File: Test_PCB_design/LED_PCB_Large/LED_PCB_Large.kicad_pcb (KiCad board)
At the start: 2 copper layers, 24 x 24 mm, 113 parts, among them J1 AS150UPB 2+4, Q1 BUK9Y107-80EX, Q10 BUK9Y107-80EX, Q11 BUK9Y107-80EX, Q12 BUK9Y107-80EX, Q2 BUK9Y107-80EX, Q3 BUK9Y107-80EX, Q4 BUK9Y107-80EX, Q5 BUK9Y107-80EX, Q6 BUK9Y107-80EX, Q7 BUK9Y107-80EX, Q8 BUK9Y107-80EX, Q9 BUK9Y107-80EX, U1 MAX20078ATE_V_T, U2 MAX20078ATE_V_T, U3 MAX20078ATE_V_T, U4 MAX20078ATE_V_T, U5 MAX20078ATE_V_T, U6 MAX20078ATE_V_T

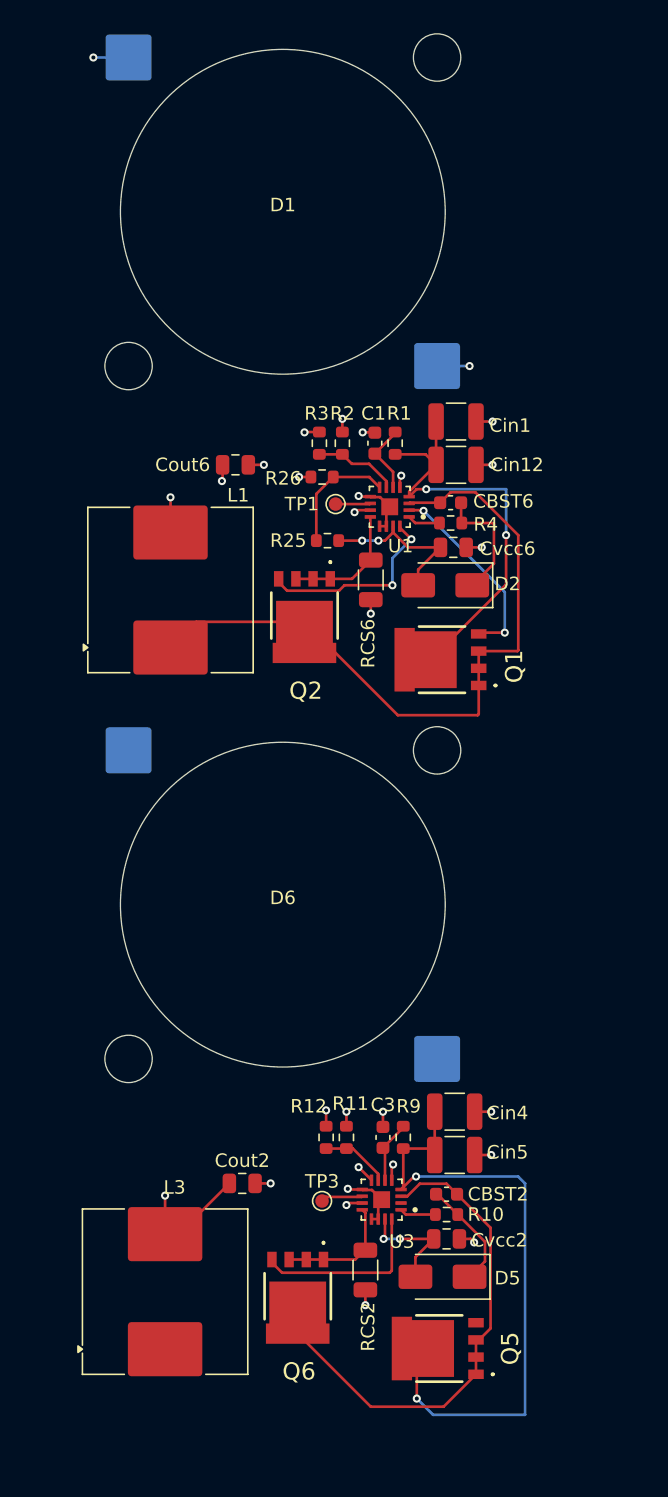
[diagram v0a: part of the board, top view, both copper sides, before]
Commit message: updated LED1 with traces
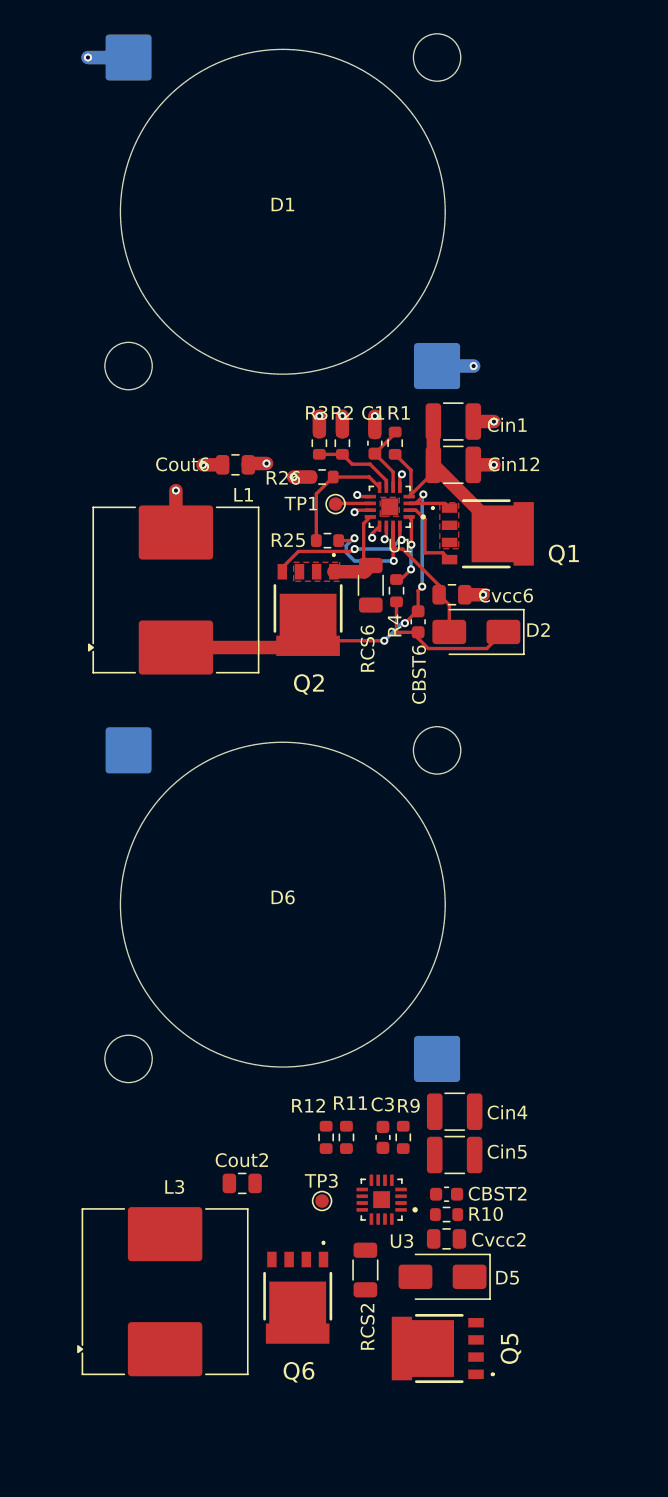
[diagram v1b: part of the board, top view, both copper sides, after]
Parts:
- moved Q1 9.86 mm to (114.5, 54.8), turned to -90 degrees
- moved CBST6 9.12 mm to (109.5, 61.3), turned to 90 degrees
- moved R4 6.40 mm to (107.9, 59.0), turned to -90 degrees
- moved D2 4.15 mm to (113.8, 62.0)
- moved Cvcc6 3.50 mm to (112.0, 59.3)
- moved Q2 0.59 mm to (101.4, 60.3)
- moved RCS6 0.40 mm to (106.0, 58.6)
- moved L1 0.40 mm to (91.6, 59.0)
- moved Cin1 0.20 mm to (112.1, 46.5)
- moved Cin12 0.20 mm to (112.1, 49.7)
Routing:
- net +48V_FUSED: track 80.2 -> 16.9 mm, vias 4 -> 0
- net Net-(Q5-S_1): track 36.2 -> 0.00 mm
- net Net-(Q1-S_1): track 52.3 -> 33.5 mm, vias 0 -> 4
- net GND: track 28.9 -> 14.9 mm, vias 18 -> 11
- net Net-(Q6-G): track 13.3 -> 0.00 mm
- net Net-(Q6-S_1): track 9.00 -> 0.00 mm
- net /LED+: track 17.6 -> 8.73 mm, vias 6 -> 4
- net Net-(Q1-G): track 14.5 -> 5.96 mm, vias 2 -> 0
- net Net-(D5-A): track 8.57 -> 0.00 mm, vias 2 -> 0
- net Net-(D5-K): track 8.28 -> 0.00 mm
- net Net-(D2-A): track 12.2 -> 18.8 mm
- net Net-(U3-OUT): track 5.09 -> 0.00 mm
- net Net-(U3-TON): track 4.67 -> 0.00 mm
- net Net-(Q2-G): track 14.5 -> 11.1 mm
- net /IOUTV3: track 3.11 -> 0.00 mm
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- added copper zone on F.Cu, net GND
- added copper zone on F.Cu, net Net-(Q1-S_1)
- added copper zone on F.Cu, net Net-(Q2-S_1)

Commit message: updated with all LED traces
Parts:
- moved L2 285.3 mm to (155.2, 58.6), turned to 90 degrees
- moved Q4 284.3 mm to (145.5, 60.4), turned to 180 degrees
- moved L4 280.5 mm to (155.2, 105.9), turned to 90 degrees
- moved L6 276.2 mm to (154.2, 153.0), turned to 90 degrees
- moved J1 274.6 mm to (123.9, 6.70), turned to 180 degrees
- moved Q8 262.0 mm to (145.5, 107.6), turned to 180 degrees
- moved U2 261.8 mm to (142.8, 52.8), turned to 180 degrees
- moved Q7 258.9 mm to (132.4, 102.9), turned to 90 degrees
- moved Q3 256.5 mm to (132.4, 55.0), turned to 90 degrees
- moved R8 249.8 mm to (146.3, 48.3), turned to 90 degrees
- moved C2 249.0 mm to (140.5, 48.3), turned to -90 degrees
- moved Cout1 248.5 mm to (151.8, 48.4), turned to 180 degrees
- moved R7 246.6 mm to (144.2, 48.3), turned to -90 degrees
- moved CBST1 246.2 mm to (137.5, 61.2), turned to 90 degrees
- moved U4 245.5 mm to (142.6, 100.2), turned to 180 degrees
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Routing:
- net +48V_FUSED: track 16.9 -> 101.8 mm, vias 0 -> 6
- net GND: track 14.9 -> 97.5 mm, vias 11 -> 66
- net /LED+: track 8.73 -> 50.6 mm, vias 4 -> 24
- net Net-(Q11-S_1): track 0.00 -> 39.9 mm
- net Net-(Q3-S_1): track 0.00 -> 39.9 mm, vias 0 -> 2
- net Net-(Q7-S_1): track 0.00 -> 39.2 mm, vias 0 -> 2
- net Net-(Q10-D_1): track 0.00 -> 33.4 mm, vias 0 -> 4
- net Net-(Q5-S_1): track 0.00 -> 33.0 mm, vias 0 -> 4
- net Net-(D7-A): track 0.00 -> 17.2 mm, vias 0 -> 4
- net Net-(D11-A): track 0.00 -> 15.3 mm, vias 0 -> 2
- net Net-(D3-A): track 0.00 -> 15.2 mm, vias 0 -> 2
- net Net-(D11-K): track 0.00 -> 13.2 mm, vias 0 -> 2
- net Net-(Q7-G): track 0.00 -> 12.3 mm, vias 0 -> 2
- net Net-(Q3-G): track 0.00 -> 12.3 mm, vias 0 -> 2
- net Net-(D3-K): track 0.00 -> 12.3 mm
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- added copper zone on F.Cu, net +48V_FUSED
- added copper zone on B.Cu, net GND
- added copper zone on F.Cu, net Net-(Q10-D_1)
- added copper zone on F.Cu, net Net-(Q10-S_1)
- added copper zone on F.Cu, net Net-(Q11-S_1)
- added copper zone on F.Cu, net Net-(Q12-S_1)
- added copper zone on F.Cu, net Net-(Q3-S_1)
- added copper zone on F.Cu, net Net-(Q4-S_1)
- added copper zone on F.Cu, net Net-(Q5-S_1)
- added copper zone on F.Cu, net Net-(Q6-S_1)
- added copper zone on F.Cu, net Net-(Q7-S_1)
- added copper zone on F.Cu, net Net-(Q8-S_1)
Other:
- board size 24 x 24 mm -> 88.7 x 182.4 mm

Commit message: updated everything just need to check electrical traces to make sure they work.
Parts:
- moved R2 8.28 mm to (96.0, 46.4), turned to 0 degrees
- moved R7 8.13 mm to (151.7, 45.1), turned to 180 degrees
- moved R11 7.83 mm to (97.9, 92.7), turned to 0 degrees
- moved F1 6.87 mm to (118.0, 20.3), turned to 90 degrees
- moved R23 6.56 mm to (151.5, 139.7), turned to 180 degrees
- moved R19 6.27 mm to (95.6, 139.5), turned to 0 degrees
- moved R15 5.70 mm to (150.4, 93.3), turned to 180 degrees
- moved C7 4.30 mm to (121.2, 27.9), turned to -90 degrees
- moved R3 1.70 mm to (104.1, 48.1)
- moved R8 1.23 mm to (145.2, 47.8)
- moved J1 0.40 mm to (123.5, 6.70)
- turned Cout5 to 180 degrees
- turned D1 to 90 degrees
- turned D10 to 90 degrees
- turned D12 to 180 degrees
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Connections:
- Cout1 pad 1: /LED+ -> /LED2+
- Cout2 pad 1: /LED+ -> /LED3+
- Cout3 pad 1: /LED+ -> /LED4+
- Cout4 pad 1: /LED+ -> /LED5+
- Cout5 pad 1: /LED+ -> /LED6+
- Cout6 pad 1: /LED+ -> /LED1+
- D1 pad 2: /LED+ -> /LED1+
- D10 pad 2: /LED+ -> /LED5+
- D12 pad 2: /LED+ -> /LED6+
- D4 pad 2: /LED+ -> /LED2+
- D6 pad 2: /LED+ -> /LED3+
- D8 pad 2: /LED+ -> /LED4+
- L1 pad 2: /LED+ -> /LED1+
- L2 pad 2: /LED+ -> /LED2+
- L3 pad 2: /LED+ -> /LED3+
- L4 pad 2: /LED+ -> /LED4+
- L5 pad 2: /LED+ -> /LED5+
- L6 pad 2: /LED+ -> /LED6+
- R11 pad 1: /LED+ -> /LED3+
- R15 pad 1: /LED+ -> /LED4+
- R19 pad 1: /LED+ -> /LED5+
- R2 pad 1: /LED+ -> /LED1+
- R23 pad 1: /LED+ -> /LED6+
- R7 pad 1: /LED+ -> /LED2+
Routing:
- net /FAULT: track 8.25 -> 386.0 mm, vias 6 -> 9
- net /PWM: track 9.17 -> 359.0 mm, vias 6 -> 7
- net /REF_1V2: track 21.1 -> 317.1 mm, vias 5 -> 13
- net /LED+: track 50.6 -> 0.00 mm, vias 24 -> 0
- net +48V_FUSED: track 101.8 -> 80.7 mm, vias 6 -> 24
- net /LED2+: track 0.00 -> 17.3 mm, vias 0 -> 2
- net /LED1+: track 0.00 -> 17.0 mm, vias 0 -> 2
- net /LED3+: track 0.00 -> 16.4 mm, vias 0 -> 2
- net /LED4+: track 0.00 -> 16.1 mm, vias 0 -> 2
- net /LED6+: track 0.00 -> 15.3 mm, vias 0 -> 2
- net /LED5+: track 0.00 -> 12.9 mm, vias 0 -> 2
- net Net-(U1-OUT): track 6.26 -> 13.0 mm
- net Net-(U6-OUT): track 9.29 -> 15.9 mm
- net Net-(U3-OUT): track 5.11 -> 11.6 mm
- net Net-(U2-OUT): track 6.77 -> 13.0 mm
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- added copper zone on In2.Cu, net +48V_FUSED
- added copper zone on F.Cu, net /LED1+
- added copper zone on F.Cu, net /LED2+
- added copper zone on F.Cu, net /LED3+
- added copper zone on F.Cu, net /LED4+
- added copper zone on F.Cu, net /LED5+
- added copper zone on F.Cu, net /LED6+
- added copper zone on In1.Cu, net GND
- added copper zone on F.Cu, net Net-(J1-+48V)
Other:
- board size 88.7 x 182.4 mm -> 85 x 170 mm
- copper layers 2 -> 4

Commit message: full done PCB (pre-pro-check)
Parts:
- added REF**: MountingHole_3.2mm_M3, MountingHole:MountingHole_3.2mm_M3, F.Cu at (88.1, 183.2)
- added REF**: MountingHole_3.2mm_M3, MountingHole:MountingHole_3.2mm_M3, F.Cu at (153.1, 24.2)
- added REF**: MountingHole_3.2mm_M3, MountingHole:MountingHole_3.2mm_M3, F.Cu at (153.1, 183.2)
- added REF**: MountingHole_3.2mm_M3, MountingHole:MountingHole_3.2mm_M3, F.Cu at (88.1, 24.2)
- moved CBST2 21.0 mm to (106.7, 130.4)
- moved Cvcc4 21.0 mm to (109.2, 174.8)
- moved Q10 21.0 mm to (98.7, 174.2)
- moved R17 21.0 mm to (104.4, 163.7)
- moved C5 21.0 mm to (102.6, 163.7)
- moved C6 21.0 mm to (136.9, 162.9)
- moved Cin9 21.0 mm to (109.8, 165.2)
- moved Cvcc5 21.0 mm to (129.2, 174.9)
- moved Q11 21.0 mm to (128.4, 170.4)
- moved Q12 21.0 mm to (141.5, 175.5)
- moved R20 21.0 mm to (99.8, 163.7)
- moved R22 21.0 mm to (135.0, 174.0)
- moved R23 21.0 mm to (148.5, 160.5)
- moved R24 21.0 mm to (140.0, 162.9)
- moved RCS4 21.0 mm to (103.3, 173.8)
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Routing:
- net GND: track 101.8 -> 163.4 mm, vias 109 -> 123
- net Net-(D11-A): track 15.3 -> 16.9 mm
- net Net-(Q11-S_1): track 39.9 -> 38.8 mm
- net Net-(D2-A): track 18.8 -> 19.5 mm
- net Net-(Q12-S_1): track 10.3 -> 11.0 mm
- net Net-(U6-BST): track 8.54 -> 7.93 mm
- net +48V_FUSED: track 80.7 -> 80.1 mm, vias 24 -> 60
